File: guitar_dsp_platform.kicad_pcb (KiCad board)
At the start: 4 copper layers, 122 x 122 mm, 143 parts, among them J201 NMJ6HCD2, J202 NMJ6HCD2, J203 NMJ6HCD2, J204 NMJ6HCD2, J401 57PC5F, J402 57PC5F, J403 I2S testpoint, J501 694106301002, Q401 2N3904, Q501 DMG2307LQ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

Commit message: Ready for layout
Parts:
- added C404: 100n, Capacitor_SMD:C_0805_2012Metric_Pad1.18x1.45mm_HandSolder, F.Cu at (218.5, 142.2)
- added C513: 3.3n, Capacitor_SMD:C_0805_2012Metric_Pad1.18x1.45mm_HandSolder, F.Cu at (176.3, 139.3)
- added C514: 100n, Capacitor_SMD:C_0805_2012Metric_Pad1.18x1.45mm_HandSolder, F.Cu at (192.7, 132.1)
- added D402: BAT760-7, Diode_SMD:D_SOD-323_HandSoldering, F.Cu at (215.1, 141.3)
- added D503: SS16-HF, Diode_SMD:D_SMA_Handsoldering, F.Cu at (195.3, 123.8)
- added FB405: 1000R@100MHz, Resistor_SMD:R_0805_2012Metric_Pad1.20x1.40mm_HandSolder, F.Cu at (220.5, 142.2)
- added R413: 10k, Resistor_SMD:R_0805_2012Metric_Pad1.20x1.40mm_HandSolder, F.Cu at (139.5, 87.2)
- added R414: 10k, Resistor_SMD:R_0805_2012Metric_Pad1.20x1.40mm_HandSolder, F.Cu at (137.5, 87.2)
- added TP301: ZERO_L, TestPoint:TestPoint_Pad_1.0x1.0mm, F.Cu at (100.2, 95.0)
- added TP302: ZERO_R, TestPoint:TestPoint_Pad_1.0x1.0mm, F.Cu at (102.2, 95.0)
- C501, C505, C511, C512: footprint Capacitor_SMD:CP_Elec_6.3x7.7 -> Capacitor_SMD:CP_Elec_6.3x5.8
- C502, C504, C507, C508, C509, C510: footprint Capacitor_SMD:C_1206_3216Metric_Pad1.33x1.80mm_HandSolder -> Capacitor_SMD:C_0805_2012Metric_Pad1.18x1.45mm_HandSolder
- C503: value 100n -> 47p
- C506: value 100n -> 3.3n
- D201, D202, D203, D204, D401: value BAT54S -> BAS40-04
- D501: value BAT54S -> SS16-HF; footprint Package_TO_SOT_SMD:SOT-23 -> Diode_SMD:D_SMA_Handsoldering
- D502: value ZMM5242B -> TZMC10-GS08
- FB201, FB202, FB401, FB402, FB403, FB404, FB501, FB502, FB503: value 600R@100MHz -> 1000R@100MHz
- J403: value I2S testpoint -> I2S
- J501: value 694106301002 -> PJ-002AH-SMT-TR; footprint Connector_BarrelJack:BarrelJack_Wuerth_6941xx301002 -> guitar_dsp_platform:CUI_PJ-002AH-SMT-TR
- L501: value 15uH -> 22u; footprint Inductor_SMD:L_Bourns-SRN8040_8x8.15mm -> Inductor_SMD:L_Taiyo-Yuden_NR-50xx_HandSoldering
- Q401: value 2N3904 -> MMBT3904; footprint Package_TO_SOT_THT:TO-92_Inline -> Package_TO_SOT_SMD:SOT-23
- Q501: value DMG2307LQ -> SI2371EDS-T1-GE3
- R205, R206, R207, R208: value DNF -> TBD
- R219, R220, R229, R231, R234: value 22k -> 20k
- R405: value 7.5k -> 820
- R501: value 1Meg -> 12.7k
- R502: value 200k -> 47k
- R504: value 121k -> 20k
- R505: value 22.1k -> 2.8k
- U201, U202, U203: value OPA2197xD -> OPA2156ID
- U501: value LMR50410 -> TPS5402; footprint Package_TO_SOT_SMD:SOT-23-6_Handsoldering -> Package_SO:SOIC-8_3.9x4.9mm_P1.27mm
- U503: value TLV74133PDBVR -> MIC5317-3.3YM5-TR; footprint Package_TO_SOT_SMD:SOT-23-5 -> Package_TO_SOT_SMD:SOT-23-5_HandSoldering
- moved R505 103.3 mm to (204.1, 101.5)
- moved C508 103.3 mm to (210.7, 101.5)
- moved C509 103.3 mm to (208.2, 101.5)
- moved C502 103.3 mm to (213.2, 101.5)
- moved R504 103.3 mm to (206.1, 101.5)
- moved TP502 100.3 mm to (196.2, 100.2)
- moved L501 97.7 mm to (209.0, 116.8), turned to 90 degrees
- moved D501 87.1 mm to (195.3, 128.4)
- moved U501 84.7 mm to (204.5, 124.8), turned to 0 degrees
- moved R501 68.5 mm to (197.4, 132.1), turned to 0 degrees
- moved R502 67.5 mm to (199.2, 145.0)
- moved C506 60.6 mm to (185.9, 139.3), turned to 0 degrees
- moved C503 41.0 mm to (181.1, 139.3)
- moved C501 8.19 mm to (141.2, 143.8), turned to 90 degrees
- moved J501 5.96 mm to (150.1, 156.7), turned to 180 degrees
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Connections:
- net /Audio Codec/VCOM_CODEC renamed /Analogue/VCOM_CODEC
- net /Audio Codec/VINL renamed /Analogue/VINL
- net /Audio Codec/VINR renamed /Analogue/VINR
- C503 pad 1: /Power Supplies/VDC_F -> /Power Supplies/SW_COMP
- C506 pad 1: /Power Supplies/SW_SW -> Net-(C506-Pad1)
- C506 pad 2: /Power Supplies/SW_BOOT -> GND
- D501 pad 1: +3V3 -> /Power Supplies/+6V_F
- D501 pad 2: /Power Supplies/+6V_F -> +5V
- J501 pad 3: (no net) -> unconnected-(J501-Pad3)
- Q401 pad 1: GND -> Net-(Q401-Pad1)
- Q401 pad 2: Net-(Q401-Pad2) -> GND
- R405 pad 1: Net-(Q401-Pad2) -> Net-(Q401-Pad1)
- R501 pad 1: /Power Supplies/VDC_F -> /Power Supplies/SW_COMP
- R501 pad 2: /Power Supplies/SW_EN -> Net-(C506-Pad1)
- R502 pad 1: /Power Supplies/SW_EN -> GND
- R502 pad 2: GND -> /Power Supplies/SW_ROSC
- R504 pad 2: /Power Supplies/SW_FB -> /Power Supplies/SW_VSENSE
- R505 pad 1: /Power Supplies/SW_FB -> /Power Supplies/SW_VSENSE
- R506 pad 2: +5V -> /Power Supplies/+5V_F
- U301 pad 1: /Audio Codec/SDA -> /ESP32/SCL
- U301 pad 2: /Audio Codec/SCL -> /ESP32/SDA
- U401 pad 19: +5V -> Net-(D402-Pad1)
- U401 pad 36: /Audio Codec/SDA -> /ESP32/SDA
- U401 pad 37: /Audio Codec/SCL -> /ESP32/SCL
- U501 pad 2: GND -> /Power Supplies/VDC_F
- U501 pad 3: /Power Supplies/SW_FB -> /Power Supplies/SW_ROSC
- U501 pad 4: /Power Supplies/SW_EN -> /Power Supplies/SW_SS
- U501 pad 5: /Power Supplies/VDC_F -> /Power Supplies/SW_VSENSE
- U501 pad 6: /Power Supplies/SW_SW -> /Power Supplies/SW_COMP
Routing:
- net /Power Supplies/VDC_IN: track 0.00 -> 16.8 mm
- net Net-(Q401-Pad1): track 0.00 -> 5.13 mm
- net Net-(Q401-Pad3): track 0.00 -> 3.35 mm
- net Net-(FB403-Pad2): track 0.00 -> 2.05 mm
- net /Power Supplies/VDC_F: track 10.2 -> 8.25 mm
- net GND: track 15.3 -> 16.6 mm, vias 95 -> 96
- net (no net): vias 0 -> 4

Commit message: Layout first draft
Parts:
- D402: value BAT760-7 -> SS16-HF; footprint Diode_SMD:D_SOD-323_HandSoldering -> Diode_SMD:D_SMA_Handsoldering
- moved C502 113.0 mm to (111.2, 150.2)
- moved FB405 108.6 mm to (112.0, 137.0), turned to 0 degrees
- moved D402 106.9 mm to (108.2, 138.0), turned to -90 degrees
- moved C404 106.5 mm to (112.0, 139.0), turned to 0 degrees
- moved R505 102.4 mm to (119.0, 158.5), turned to 180 degrees
- moved R504 101.0 mm to (122.8, 158.5), turned to 180 degrees
- moved C508 97.8 mm to (120.8, 140.0), turned to 180 degrees
- moved C509 96.4 mm to (120.8, 142.0), turned to 180 degrees
- moved U501 92.2 mm to (116.5, 152.3)
- moved L501 90.5 mm to (123.8, 147.0)
- moved R502 90.3 mm to (109.5, 155.2), turned to 90 degrees
- moved TP502 82.5 mm to (124.5, 141.0)
- moved D503 81.9 mm to (116.2, 145.2), turned to 180 degrees
- moved R501 78.1 mm to (122.8, 155.0)
- moved C514 75.9 mm to (118.5, 148.2)
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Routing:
- net /ESP32/SCL: track 0.00 -> 92.2 mm, vias 0 -> 2
- net Net-(D402-Pad1): track 0.00 -> 88.4 mm, vias 0 -> 1
- net /ESP32/SDA: track 0.00 -> 85.5 mm, vias 0 -> 2
- net VDD: track 155.1 -> 234.0 mm, vias 7 -> 11
- net /ESP32/MIDI_TX_uC: track 0.00 -> 64.0 mm, vias 0 -> 1
- net /ESP32/MIDI_RX_uC: track 0.00 -> 62.6 mm, vias 0 -> 1
- net +5VA: track 160.7 -> 219.4 mm
- net +3V3: track 8.93 -> 63.1 mm, vias 0 -> 2
- net +6V: track 0.00 -> 51.3 mm
- net /Power Supplies/VDC_F: track 8.25 -> 47.8 mm, vias 0 -> 2
- net +5V: track 0.00 -> 33.6 mm
- net GND: track 16.6 -> 45.4 mm, vias 96 -> 159
- net /Power Supplies/SW_SW: track 0.00 -> 17.9 mm
- net /ESP32/LED-: track 0.00 -> 16.9 mm
- net Net-(FB402-Pad2): track 0.00 -> 16.8 mm
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
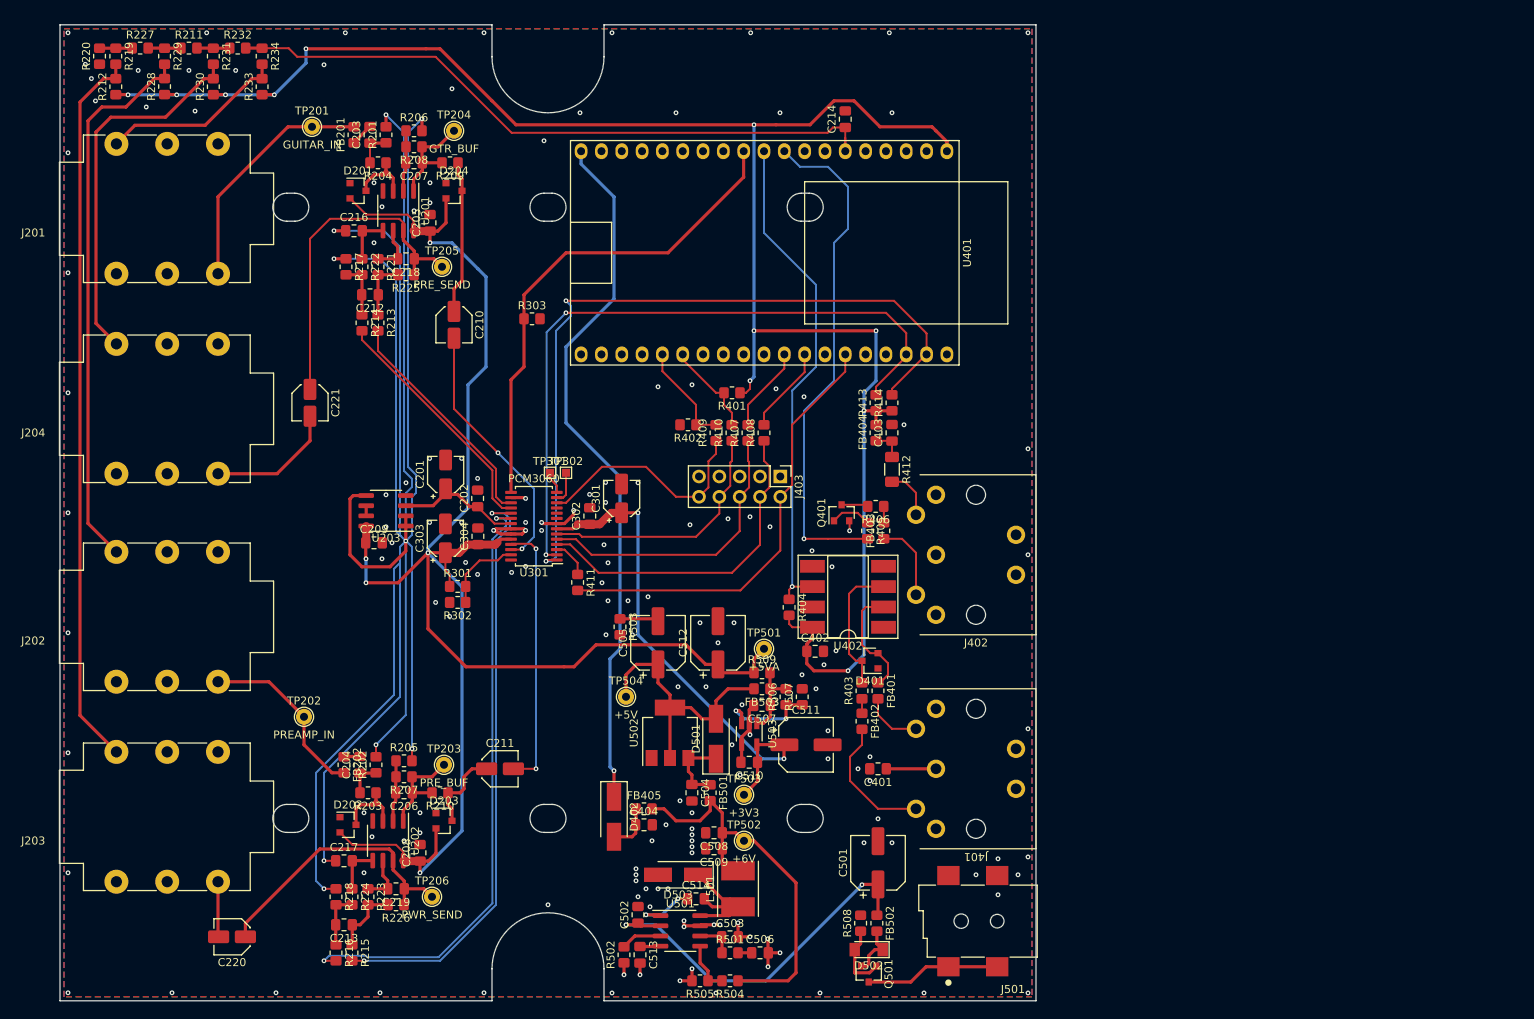
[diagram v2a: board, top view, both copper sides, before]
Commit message: Mechanical tweaks of I/O
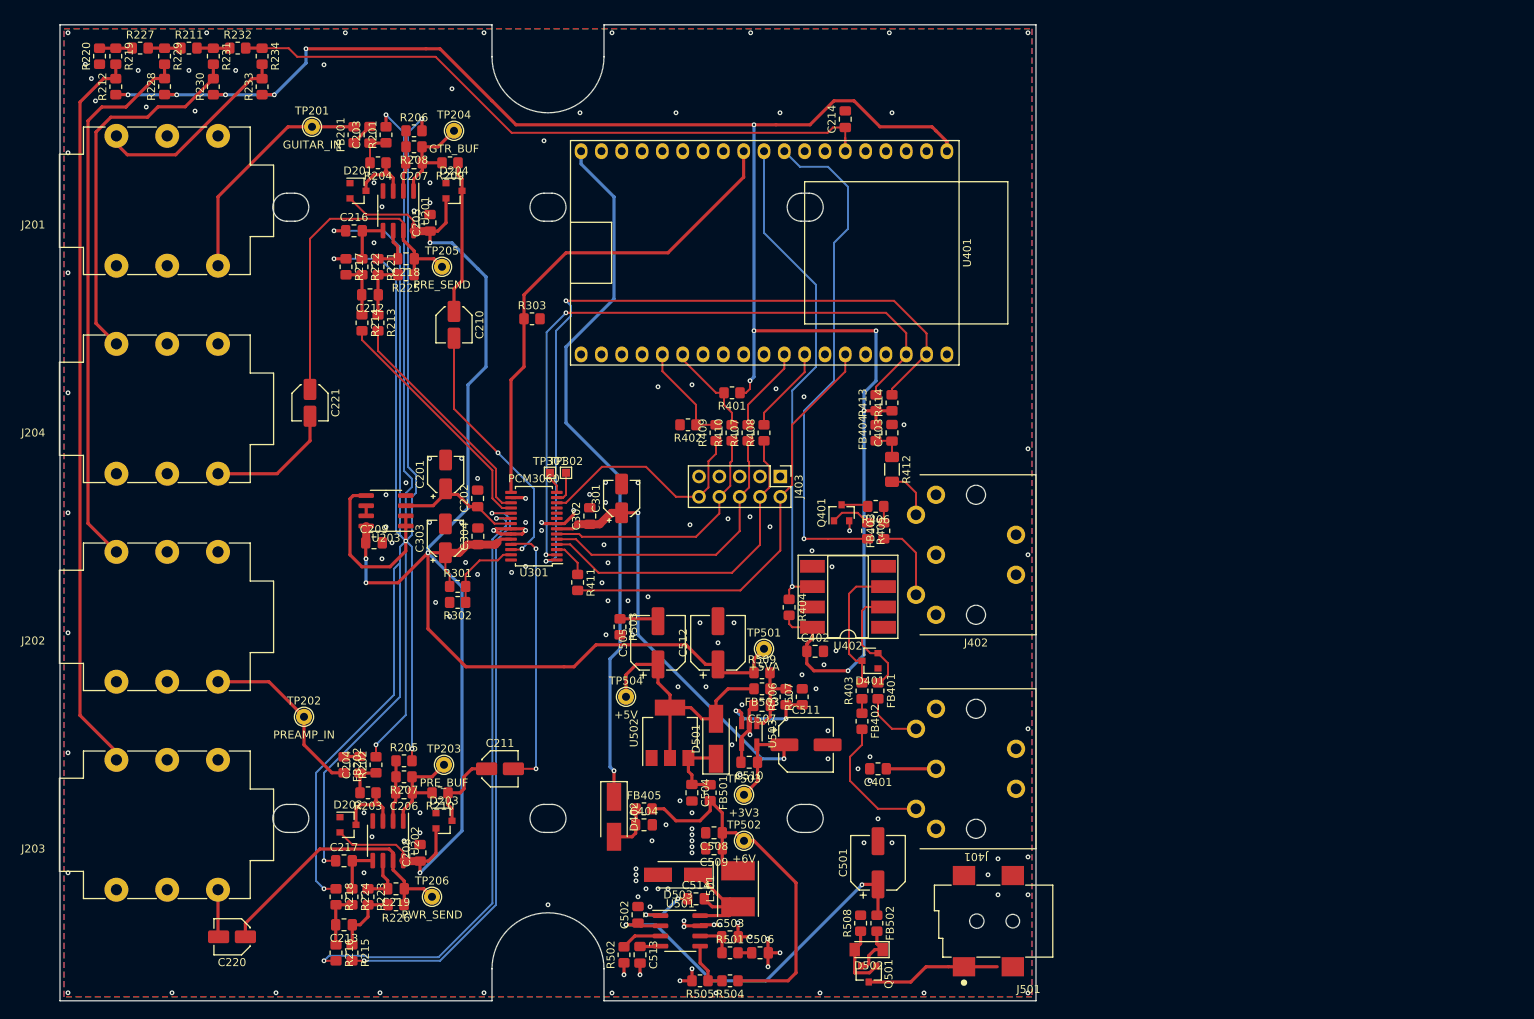
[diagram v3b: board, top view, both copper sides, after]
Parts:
- moved J501 1.95 mm to (152.0, 156.7)
- moved J201 1.00 mm to (42.0, 61.0)
- moved J203 1.00 mm to (42.0, 139.0)
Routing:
- net /Analogue/G_DET_JACK: track 23.4 -> 24.5 mm
- net Net-(FB201-Pad2): track 30.4 -> 29.4 mm
- net Net-(C220-Pad2): track 6.92 -> 5.92 mm

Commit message: Clean up layout, add testpoints, layer markers
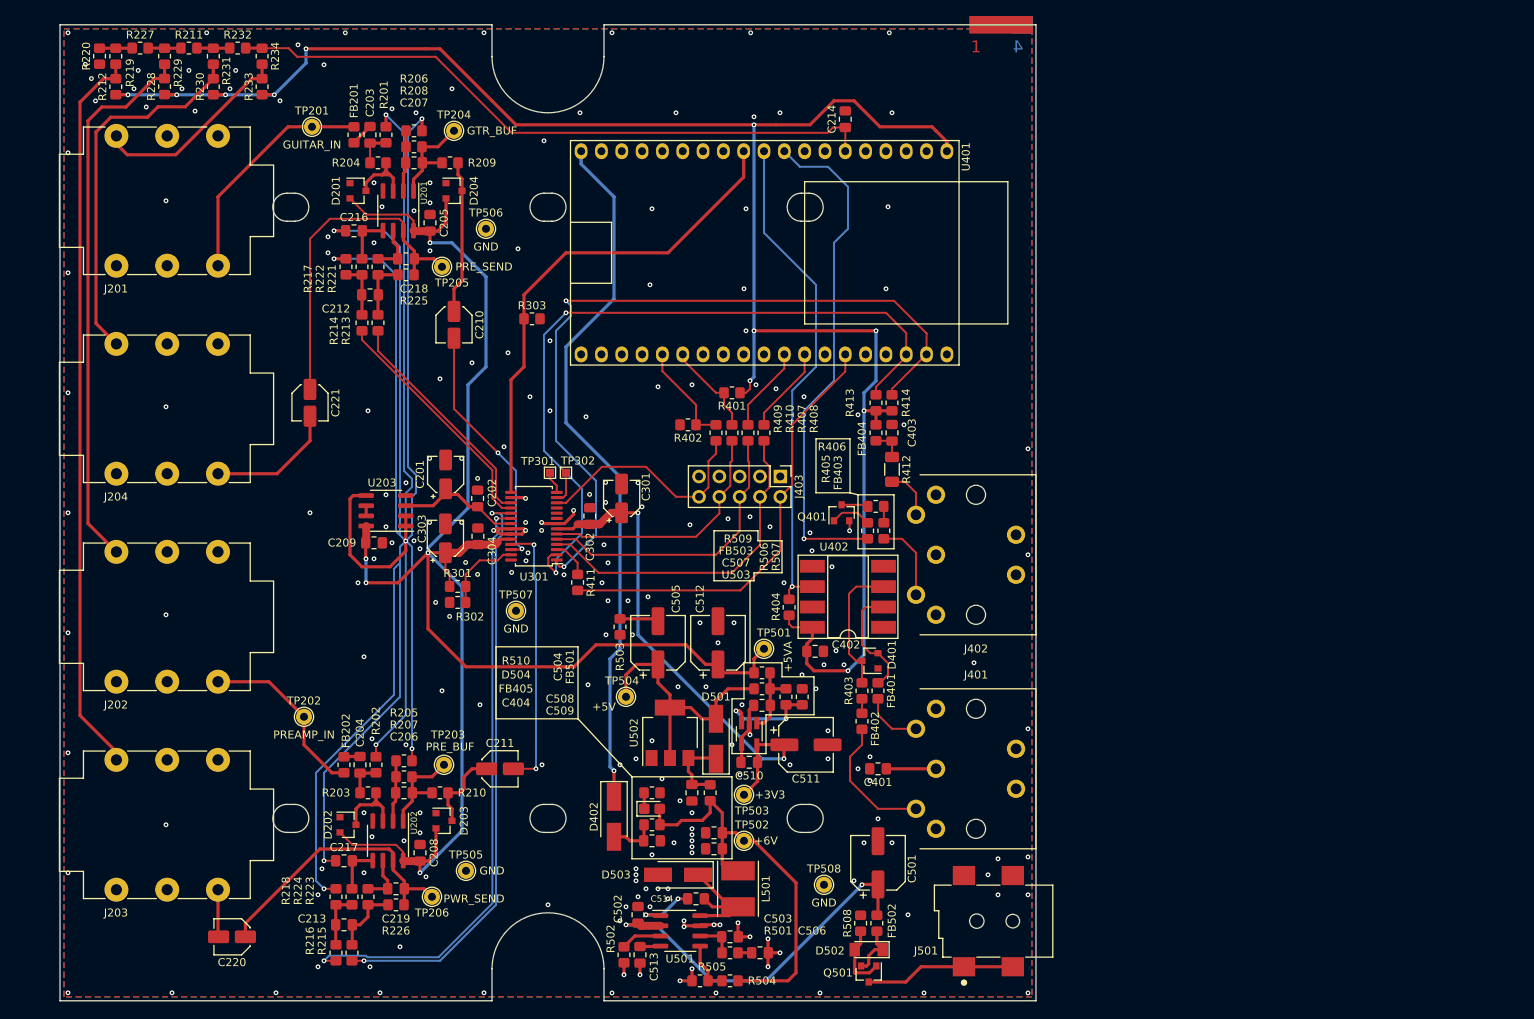
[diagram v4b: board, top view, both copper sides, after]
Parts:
- added D504: LS R976-NR-1, LED_SMD:LED_0805_2012Metric_Castellated, F.Cu at (113.0, 137.0)
- added R510: 10k, Resistor_SMD:R_0805_2012Metric_Pad1.20x1.40mm_HandSolder, F.Cu at (113.0, 135.0)
- added TP505: GND, guitar_dsp_platform:TestPoint_THTPad_D2.0mm_Drill1.0mm, F.Cu at (89.8, 144.8)
- added TP506: GND, guitar_dsp_platform:TestPoint_THTPad_D2.0mm_Drill1.0mm, F.Cu at (92.2, 64.5)
- added TP507: GND, guitar_dsp_platform:TestPoint_THTPad_D2.0mm_Drill1.0mm, F.Cu at (96.0, 112.2)
- added TP508: GND, guitar_dsp_platform:TestPoint_THTPad_D2.0mm_Drill1.0mm, F.Cu at (134.5, 146.5)
- moved C404 2.24 mm to (113.0, 141.0)
- moved FB405 2.24 mm to (113.0, 139.0)
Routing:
- net GND: track 45.4 -> 145.2 mm, vias 159 -> 226
- net /ESP32/SDA: track 85.5 -> 93.3 mm
- net /ESP32/SCL: track 92.2 -> 95.8 mm
- net Net-(D504-Pad1): track 0.00 -> 2.02 mm
- net /Power Supplies/VDC_IN: track 16.8 -> 18.8 mm
- net /Analogue/JACK_DETECT: track 84.2 -> 82.6 mm
- net /Power Supplies/SW_SW: track 17.9 -> 16.5 mm
- net /Analogue/VOUTL+: track 77.3 -> 76.1 mm
- net /Analogue/VINR: track 32.5 -> 31.3 mm
- net /Analogue/VOUTL-: track 74.8 -> 73.6 mm
- net +6V: track 51.3 -> 52.0 mm
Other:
- board text added: "1"
- board text added: "2"
- board text added: "3"
- board text added: "4"
